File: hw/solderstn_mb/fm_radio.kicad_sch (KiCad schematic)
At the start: 20 parts, among them J2201 Conn_01x02, J2202 Molex_PicoBlade-53398-0271, J2203 Conn_Coaxial, J2204 alt-placement, U2201 Si4735-D60-GU

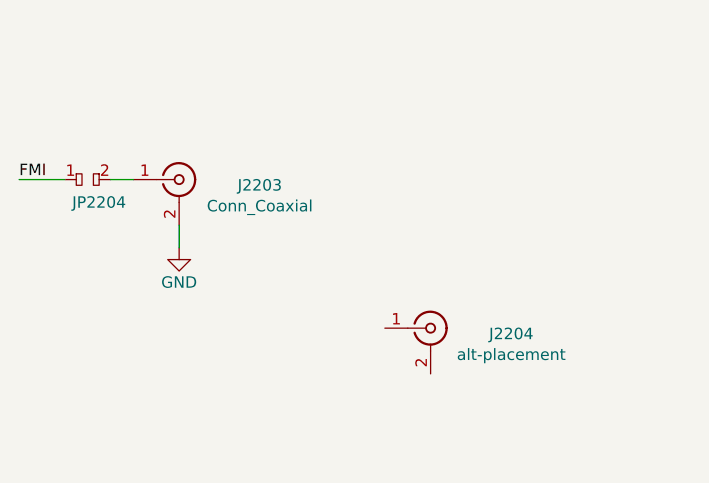
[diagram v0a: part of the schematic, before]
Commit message: Placeholder 3d-models for rear-panel (w. conns), PSU, Bottom-plate, front-panel (w. conns), outer fp
With these placeholder mech. objects, the build-in 3d view of MB pcb features most of the mechanical
objects that constrain components placements. So 3d-view can be used to quickly check and iterate
placements to avoid 3d collisions, without having to first export MB STEP into FreeCAD and muck around
only to have to repeat again for each iteration
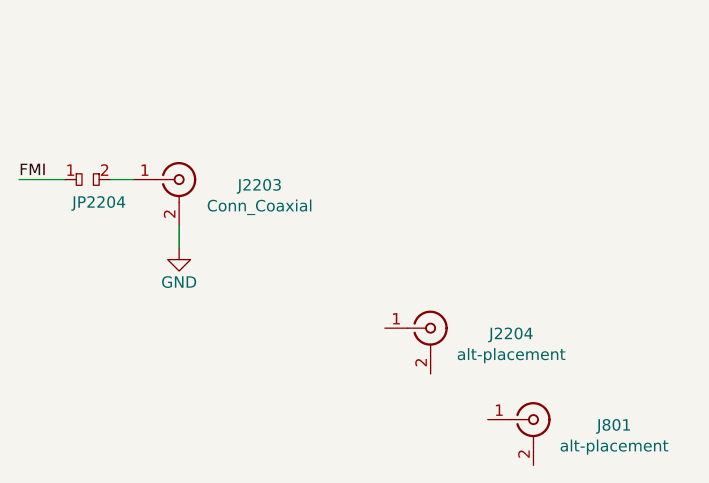
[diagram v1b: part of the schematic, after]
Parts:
- added J801: alt-placement, customlib_mj_fp:SMA_Molex_73251-2200_Horizontal, symbol Connector:Conn_Coaxial
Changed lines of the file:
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@@
     )
   )
-  (symbol (lib_id "Connector:Conn_Coaxial") (at 242.57 139.7 0)
+  (symbol (lib_id "Connector:Conn_Coaxial") (at 242.57 139.7 0) (unit 1)
     (in_bom yes) (on_board yes)
     (property "Reference" "J2204" (id 0) (at 251.5362 140.335 0))
@@
     (pin "2")
   )
-  (symbol (lib_id "RF_AM_FM:Si4735-D60-GU") (at 113.03 77.47 0)
+  (symbol (lib_id "RF_AM_FM:Si4735-D60-GU") (at 113.03 77.47 0) (unit 1)
     (in_bom yes) (on_board yes)
     (property "Reference" "U2201" (id 0) (at 105.41 95.25 0)
@@
     (pin "9")
   )
-  (symbol (lib_id "power:VDDA") (at 115.57 43.18 0)
+  (symbol (lib_id "power:VDDA") (at 115.57 43.18 0) (unit 1)
     (in_bom yes) (on_board yes)
     (property "Reference" "#PWR02202" (id 0) (at 115.57 46.99 0)
@@
     (pin "1")
   )
-  (symbol (lib_id "power:VDD") (at 76.2 60.96 0)
+  (symbol (lib_id "power:VDD") (at 76.2 60.96 0) (unit 1)
     (in_bom yes) (on_board yes)
     (property "Reference" "#PWR02204" (id 0) (at 76.2 64.77 0)
@@
     (pin "1")
   )
-  (symbol (lib_id "Device:C_Small") (at 120.65 48.26 0)
+  (symbol (lib_id "Device:C_Small") (at 120.65 48.26 0) (unit 1)
     (in_bom yes) (on_board yes)
     (property "Reference" "C2202" (id 0) (at 121.92 45.72 0)
@@
     (pin "2")
   )
-  (symbol (lib_id "Device:C_Small") (at 105.41 48.26 0) (mirror y)
+  (symbol (lib_id "Device:C_Small") (at 105.41 48.26 0) (mirror y) (unit 1)
     (in_bom yes) (on_board yes)
     (property "Reference" "C2201" (id 0) (at 104.14 45.72 0)
@@
     (pin "2")
   )
-  (symbol (lib_id "power:GND") (at 105.41 52.07 0)
+  (symbol (lib_id "power:GND") (at 105.41 52.07 0) (unit 1)
     (in_bom yes) (on_board yes)
     (property "Reference" "#PWR02203" (id 0) (at 105.41 58.42 0)
@@
     (pin "1")
   )
-  (symbol (lib_id "power:GND") (at 66.04 69.85 0)
+  (symbol (lib_id "power:GND") (at 66.04 69.85 0) (unit 1)
     (in_bom yes) (on_board yes)
     (property "Reference" "#PWR02205" (id 0) (at 66.04 76.2 0)
@@
     (pin "1")
   )
-  (symbol (lib_id "power:GND") (at 115.57 101.6 0)
+  (symbol (lib_id "power:GND") (at 115.57 101.6 0) (unit 1)
     (in_bom yes) (on_board yes)
     (property "Reference" "#PWR02212" (id 0) (at 115.57 107.95 0)
@@
     (pin "1")
   )
-  (symbol (lib_id "power:GND") (at 110.49 101.6 0)
+  (symbol (lib_id "power:GND") (at 110.49 101.6 0) (unit 1)
     (in_bom yes) (on_board yes)
     (property "Reference" "#PWR02211" (id 0) (at 110.49 107.95 0)
@@
     (pin "1")
   )
-  (symbol (lib_id "Device:R_Small") (at 134.62 69.85 270)
+  (symbol (lib_id "Device:R_Small") (at 134.62 69.85 270) (unit 1)
     (in_bom yes) (on_board yes)
     (property "Reference" "R2201" (id 0) (at 137.16 68.58 90)
@@
     (pin "2")
   )
-  (symbol (lib_id "Device:R_Small") (at 134.62 77.47 270)
+  (symbol (lib_id "Device:R_Small") (at 134.62 77.47 270) (unit 1)
     (in_bom yes) (on_board yes)
     (property "Reference" "R2202" (id 0) (at 137.16 76.2 90)
@@
     (pin "2")
   )
-  (symbol (lib_id "Device:R_Small") (at 91.44 82.55 90) (mirror x)
+  (symbol (lib_id "Device:R_Small") (at 91.44 82.55 90) (mirror x) (unit 1)
     (in_bom yes) (on_board yes)
     (property "Reference" "R2203" (id 0) (at 88.9 81.28 90)
@@
     (pin "2")
   )
-  (symbol (lib_id "power:GND") (at 130.81 101.6 0)
+  (symbol (lib_id "power:GND") (at 130.81 101.6 0) (unit 1)
     (in_bom yes) (on_board yes)
     (property "Reference" "#PWR02213" (id 0) (at 130.81 107.95 0)
@@
     (pin "1")
   )
-  (symbol (lib_id "Device:C_Small") (at 161.29 72.39 0)
+  (symbol (lib_id "Device:C_Small") (at 161.29 72.39 0) (unit 1)
     (in_bom yes) (on_board yes)
     (property "Reference" "C2203" (id 0) (at 162.56 69.85 0)
@@
     (pin "2")
   )
-  (symbol (lib_id "power:GND") (at 171.45 69.85 0)
+  (symbol (lib_id "power:GND") (at 171.45 69.85 0) (unit 1)
     (in_bom yes) (on_board yes)
     (property "Reference" "#PWR02206" (id 0) (at 171.45 76.2 0)
@@
     (pin "1")
   )
-  (symbol (lib_id "power:VDD") (at 110.49 43.18 0)
+  (symbol (lib_id "power:VDD") (at 110.49 43.18 0) (unit 1)
     (in_bom yes) (on_board yes)
     (property "Reference" "#PWR02201" (id 0) (at 110.49 46.99 0)
@@
     (pin "1")
   )
-  (symbol (lib_id "Device:C_Small") (at 144.78 85.09 270)
+  (symbol (lib_id "Device:C_Small") (at 144.78 85.09 270) (unit 1)
     (in_bom yes) (on_board yes)
     (property "Reference" "C2205" (id 0) (at 146.05 83.82 90)
@@
     (pin "2")
   )
-  (symbol (lib_id "Connector_Generic:Conn_01x02") (at 214.63 81.28 0)
+  (symbol (lib_id "Connector_Generic:Conn_01x02") (at 214.63 81.28 0) (unit 1)
     (in_bom yes) (on_board yes)
     (property "Reference" "J2201" (id 0) (at 217.17 81.28 0)
@@
     (pin "2")
   )
-  (symbol (lib_id "Device:C_Small") (at 152.4 81.28 270)
+  (symbol (lib_id "Device:C_Small") (at 152.4 81.28 270) (unit 1)
     (in_bom yes) (on_board yes)
     (property "Reference" "C2204" (id 0) (at 153.67 80.01 90)
@@
     (pin "2")
   )
-  (symbol (lib_id "Device:L_Small") (at 135.89 90.17 0)
+  (symbol (lib_id "Device:L_Small") (at 135.89 90.17 0) (unit 1)
     (in_bom yes) (on_board yes)
     (property "Reference" "L2201" (id 0) (at 137.1092 89.0016 0)
@@
     (pin "2")
   )
-  (symbol (lib_id "Power_Protection:CM1213A-01SO") (at 161.29 99.06 0) (mirror x)
+  (symbol (lib_id "Power_Protection:CM1213A-01SO") (at 161.29 99.06 0) (mirror x) (unit 1)
     (in_bom yes) (on_board yes)
     (property "Reference" "D2202" (id 0) (at 161.29 104.14 0))
@@
     (pin "3")
   )
-  (symbol (lib_id "power:GND") (at 135.89 101.6 0)
+  (symbol (lib_id "power:GND") (at 135.89 101.6 0) (unit 1)
     (in_bom yes) (on_board yes)
     (property "Reference" "#PWR02214" (id 0) (at 135.89 107.95 0)
@@
     (pin "1")
   )
-  (symbol (lib_id "power:GND") (at 154.94 101.6 0)
+  (symbol (lib_id "power:GND") (at 154.94 101.6 0) (unit 1)
     (in_bom yes) (on_board yes)
     (property "Reference" "#PWR02215" (id 0) (at 154.94 107.95 0)
@@
     (pin "1")
   )
-  (symbol (lib_id "power:GND") (at 167.64 101.6 0)
+  (symbol (lib_id "power:GND") (at 167.64 101.6 0) (unit 1)
     (in_bom yes) (on_board yes)
     (property "Reference" "#PWR02216" (id 0) (at 167.64 107.95 0)
@@
     (pin "1")
   )
-  (symbol (lib_id "Power_Protection:CM1213A-01SO") (at 199.39 90.17 0) (mirror x)
+  (symbol (lib_id "Power_Protection:CM1213A-01SO") (at 199.39 90.17 0) (mirror x) (unit 1)
     (in_bom yes) (on_board yes)
     (property "Reference" "D2201" (id 0) (at 199.39 95.25 0))
@@
     (pin "3")
   )
-  (symbol (lib_id "power:GND") (at 193.04 91.44 0)
+  (symbol (lib_id "power:GND") (at 193.04 91.44 0) (unit 1)
     (in_bom yes) (on_board yes)
     (property "Reference" "#PWR02209" (id 0) (at 193.04 97.79 0)
@@
     (pin "1")
   )
-  (symbol (lib_id "power:GND") (at 205.74 91.44 0)
+  (symbol (lib_id "power:GND") (at 205.74 91.44 0) (unit 1)
     (in_bom yes) (on_board yes)
     (property "Reference" "#PWR02210" (id 0) (at 205.74 97.79 0)
@@
     (pin "1")
   )
-  (symbol (lib_id "power:GND") (at 207.01 85.09 0)
+  (symbol (lib_id "power:GND") (at 207.01 85.09 0) (unit 1)
     (in_bom yes) (on_board yes)
     (property "Reference" "#PWR02207" (id 0) (at 207.01 91.44 0)
@@
     (pin "1")
   )
-  (symbol (lib_id "Connector_Generic:Conn_01x02") (at 179.07 85.09 0)
+  (symbol (lib_id "Connector_Generic:Conn_01x02") (at 179.07 85.09 0) (unit 1)
     (in_bom yes) (on_board yes)
     (property "Reference" "J2202" (id 0) (at 179.07 90.17 0))
@@
     (pin "2")
   )
-  (symbol (lib_id "power:GND") (at 165.1 90.17 0)
+  (symbol (lib_id "power:GND") (at 165.1 90.17 0) (unit 1)
     (in_bom yes) (on_board yes)
     (property "Reference" "#PWR02208" (id 0) (at 165.1 96.52 0)
@@
     (pin "1")
   )
-  (symbol (lib_id "customlib_mj:dogbone_3_ud") (at 71.12 63.5 0)
+  (symbol (lib_id "customlib_mj:dogbone_3_ud") (at 71.12 63.5 0) (unit 1)
     (in_bom yes) (on_board yes)
     (property "Reference" "JP2201" (id 0) (at 71.12 60.1218 0))
@@
     (pin "3")
   )
-  (symbol (lib_id "customlib_mj:dogbone_2_ud") (at 92.71 69.85 0)
+  (symbol (lib_id "customlib_mj:dogbone_2_ud") (at 92.71 69.85 0) (unit 1)
     (in_bom yes) (on_board yes)
     (property "Reference" "JP2202" (id 0) (at 92.71 66.4464 0))
@@
     (pin "2")
   )
-  (symbol (lib_id "customlib_mj:dogbone_2_ud") (at 168.91 85.09 0)
+  (symbol (lib_id "customlib_mj:dogbone_2_ud") (at 168.91 85.09 0) (unit 1)
     (in_bom yes) (on_board yes)
     (property "Reference" "JP2203" (id 0) (at 168.91 86.36 0))
@@
     (pin "2")
   )
-  (symbol (lib_id "Connector:Conn_Coaxial") (at 214.63 123.19 0)
+  (symbol (lib_id "Connector:Conn_Coaxial") (at 214.63 123.19 0) (unit 1)
     (in_bom yes) (on_board yes)
     (property "Reference" "J2203" (id 0) (at 223.5962 123.825 0))
@@
     (pin "2")
   )
-  (symbol (lib_id "power:GND") (at 214.63 130.81 0)
+  (symbol (lib_id "power:GND") (at 214.63 130.81 0) (unit 1)
     (in_bom yes) (on_board yes)
     (property "Reference" "#PWR02217" (id 0) (at 214.63 137.16 0)
@@
     (pin "1")
   )
-  (symbol (lib_id "customlib_mj:dogbone_2_ud") (at 204.47 123.19 0)
+  (symbol (lib_id "customlib_mj:dogbone_2_ud") (at 204.47 123.19 0) (unit 1)
     (in_bom yes) (on_board yes)
     (property "Reference" "JP2204" (id 0) (at 205.74 125.73 0))
@@
       (effects (font (size 1.27 1.27)) hide)
     )
+    (pin "1")
+    (pin "2")
+  )
+  (symbol (lib_id "Connector:Conn_Coaxial") (at 254 149.86 0) (unit 1)
+    (in_bom yes) (on_board yes)
+    (property "Reference" "J801" (id 0) (at 262.9662 150.495 0))
+    (property "Value" "alt-placement" (id 1) (at 262.9662 152.8064 0))
+    (property "Footprint" "customlib_mj_fp:SMA_Molex_73251-2200_Horizontal" (id 2) (at 254 149.86 0)
+      (effects (font (size 1.27 1.27)) hide)
+    )
+    (property "Datasheet" " ~" (id 3) (at 254 149.86 0)
+      (effects (font (size 1.27 1.27)) hide)
+    )

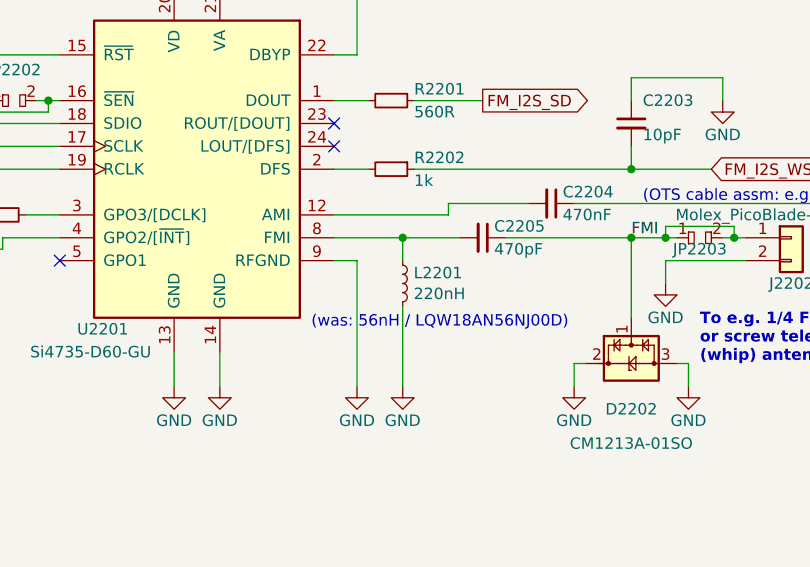
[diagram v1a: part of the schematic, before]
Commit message: hw: long-standing uncommitted stuff; mostly auto-updates (v7) fw: remove L052 tree (CMSIS & std-HAL shouldn't be committed and it was the wrong device name anyway)
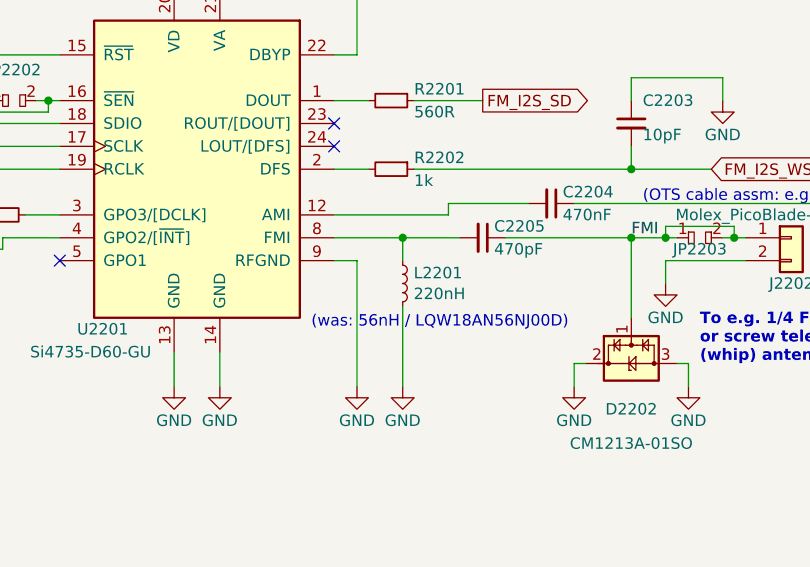
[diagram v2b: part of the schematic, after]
